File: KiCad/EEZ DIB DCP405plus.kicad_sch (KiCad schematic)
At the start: 21 parts

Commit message: Basic front mask gerbers, two test points, BOM updated
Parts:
- added TR1: EPP-150-48, symbol PCM_EEZ_unsorted:AC-DC module
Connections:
- no-connect marks 0 -> 4
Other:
- note added: "Alternative: Mean Well LOP-200-48"
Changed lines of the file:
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@@
 	(title_block
 		(title "${project_name}")
-		(date "2026-09-19")
+		(date "2026-09-20")
 		(rev "${project_version}")
 		(company "${project_creator}")
@@
 		(comment 2 "${project_info}")
 		(comment 3 "${project_url}")
+	)
+	(text "Alternative: Mean Well LOP-200-48"
+		(exclude_from_sim no)
+		(at 106.68 179.07 0)
+		(effects
+			(font
+				(size 0.889 0.889)
+				(color 132 0 132 1)
+			)
+			(justify left bottom)
+		)
 	)
 	(text "HR000120"
@@
 			)
 		)
+	)
+	(no_connect
+		(at 104.14 160.02)
+	)
+	(no_connect
+		(at 129.54 162.56)
+	)
+	(no_connect
+		(at 104.14 170.18)
+	)
+	(no_connect
+		(at 129.54 167.64)
 	)
 	(symbol
@@
 					(unit 1)
 				)
+			)
+		)
+	)
+	(symbol
+		(lib_id "PCM_EEZ_unsorted:AC-DC module")
+		(at 116.84 165.1 0)
+		(unit 1)
+		(body_style 1)
+		(exclude_from_sim no)
+		(in_bom yes)
+		(on_board no)
+		(in_pos_files no)
+		(dnp no)
+		(fields_autoplaced yes)
+		(property "Reference" "TR1"
+			(at 106.68 154.305 0)
+			(show_name no)
+			(do_not_autoplace yes)
+			(effects
+				(font
+					(size 1.27 1.27)
+				)
+				(justify left bottom)
+			)
+		)
+		(property "Value" "EPP-150-48"
+			(at 106.68 175.895 0)
+			(show_name no)
+			(do_not_autoplace yes)
+			(effects
+				(font
+					(size 1.27 1.27)
+				)
+				(justify left top)
+			)
+		)
+		(property "Footprint" ""
+			(at 116.84 178.435 0)
+			(hide yes)
+			(show_name no)
+			(do_not_autoplace no)
+			(effects
+				(font
+					(size 1.27 1.27)
+				)
+			)
+		)
+		(property "Datasheet" ""
+			(at 116.84 165.1 0)
+			(hide yes)
+			(show_name no)
+			(do_not_autoplace no)
+			(effects
+				(font
+					(size 1.27 1.27)
+				)
+			)
+		)
+		(property "Description" ""
+			(at 116.84 165.1 0)
+			(hide yes)
+			(show_name no)
+			(do_not_autoplace no)
+			(effects
+				(font
+					(size 1.27 1.27)
+				)
+			)
+		)
+		(property "DigiKey" "1866-1644-ND"
+			(at 116.84 165.1 0)
+			(hide yes)
+			(show_name no)
+			(do_not_autoplace no)
+			(effects
+				(font
+					(size 0.889 0.889)
+				)
+			)
+		)
+		(property "Mouser" "709-EPP150-48"
+			(at 116.84 165.1 0)
+			(hide yes)
+			(show_name no)
+			(do_not_autoplace no)
+			(effects
+				(font
+					(size 0.889 0.889)
+				)
+			)
+		)
+		(property "TME" "EPP-150-48"
+			(at 116.84 165.1 0)
+			(hide yes)
+			(show_name no)
+			(do_not_autoplace no)
+			(effects
+				(font
+					(size 0.889 0.889)
+				)
+			)
+		)
+		(property "LCSC" "C5729605"
+			(at 116.84 165.1 0)
+			(hide yes)
+			(show_name no)
+			(do_not_autoplace no)
+			(effects
+				(font
+					(size 0.889 0.889)
+				)
+			)
+		)
+		(pin "ACL"
+		)
+		(pin "V+"
+		)
+		(pin "ACN"
+		)
+		(pin "V-"
+		)
+		(instances
+			(project "EEZ DIB DCP405plus"
+				(path "/65943c0e-8943-4d2a-93dc-fb4938f73312"
+					(reference "TR1")
+					(unit 1)
+				)

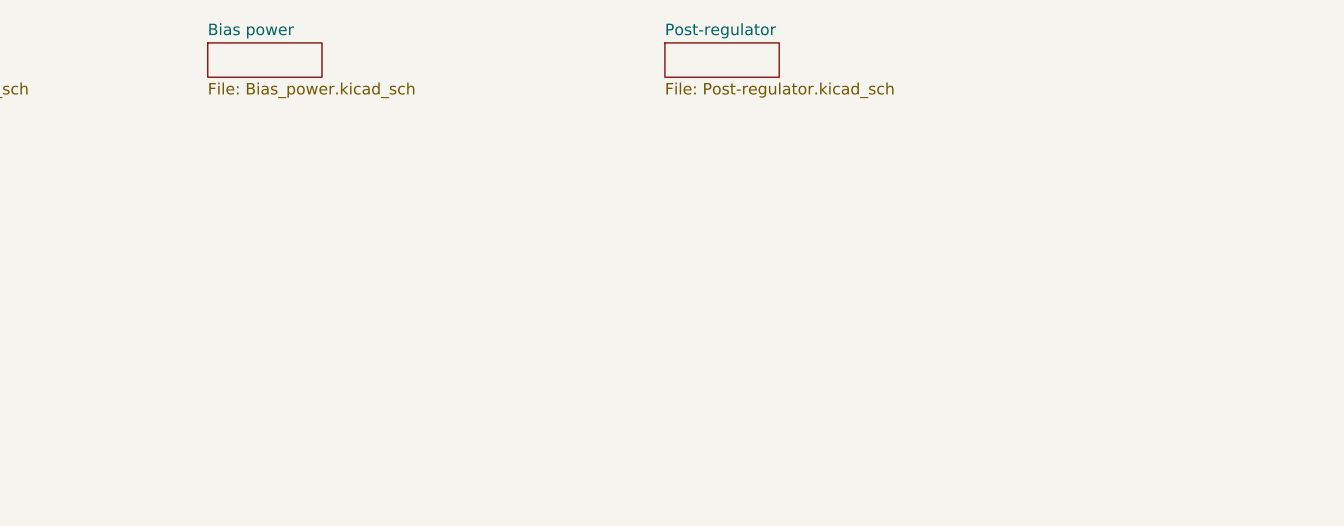
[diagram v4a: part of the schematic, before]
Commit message: Front masks added into main schematics
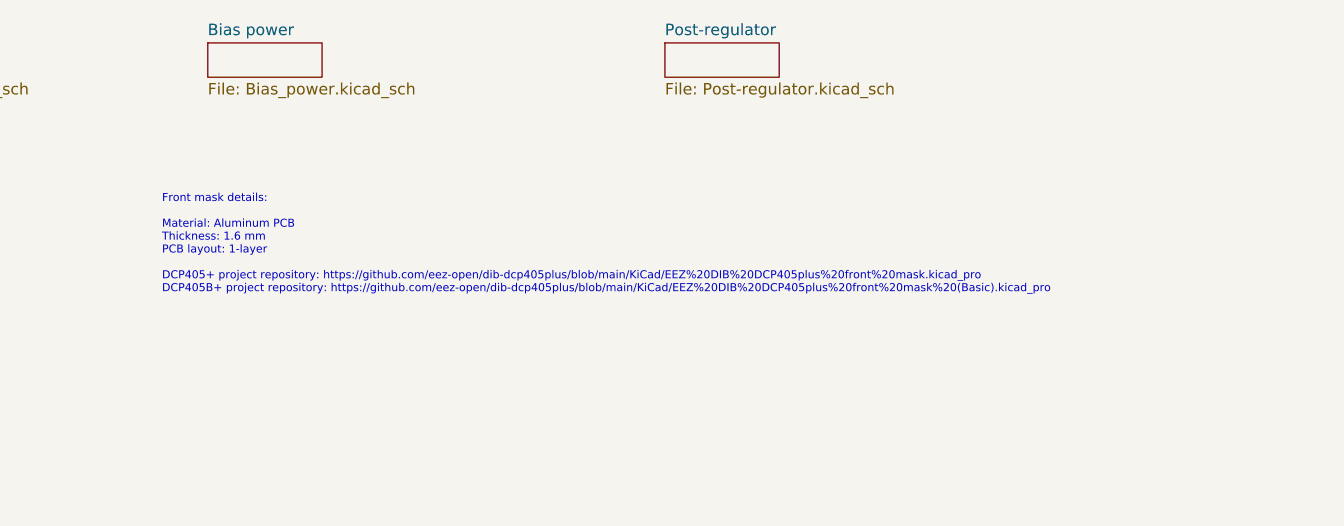
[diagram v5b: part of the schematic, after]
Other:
- note added: "Front mask details: Material: Aluminum PCB Thickness: 1.6 mm PCB layout: 1-layer DCP405+ project repository: https://github.com/eez-open/dib-dcp405plus/blob/main/KiCad/EEZ%20DIB%20DCP405plus%20front%20mask.kicad_pro DCP405B+ project repository: https://github.com/eez-open/dib-dcp405plus/blob/main/KiCad/EEZ%20DIB%20DCP405plus%20front%20mask%20(Basic).kicad_pro"

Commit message: BOM update
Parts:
- TR1: DigiKey 1866-1644-ND -> 1866-1644-ND or 1866-LOP-200-48-ND; LCSC C5729605 -> C5729605 or C28871933; Mouser 709-EPP150-48 -> 709-EPP150-48 or 709-LOP-200-48; TME EPP-150-48 -> EPP-150-48 or LOP-200-48
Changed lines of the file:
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@@
 			)
 		)
-		(property "DigiKey" "1866-1644-ND"
+		(property "DigiKey" "1866-1644-ND or 1866-LOP-200-48-ND"
 			(at 116.84 165.1 0)
 			(hide yes)
@@
 			)
 		)
-		(property "Mouser" "709-EPP150-48"
+		(property "Mouser" "709-EPP150-48 or 709-LOP-200-48"
 			(at 116.84 165.1 0)
 			(hide yes)
@@
 			)
 		)
-		(property "TME" "EPP-150-48"
+		(property "TME" "EPP-150-48 or LOP-200-48"
 			(at 116.84 165.1 0)
 			(hide yes)
@@
 			)
 		)
-		(property "LCSC" "C5729605"
+		(property "LCSC" "C5729605 or C28871933"
 			(at 116.84 165.1 0)
 			(hide yes)
